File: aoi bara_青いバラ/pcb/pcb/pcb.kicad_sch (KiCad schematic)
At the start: 200 parts, among them J1 OLED_128x64, U1 Raspberry_Pi_Pico

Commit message: deleted:    "aoi bara_\351\235\222\343\201\204\343\203\220\343\203\251/pcb/pcb/#auto_saved_files#" 	deleted:    "aoi bara_\351\235\222\343\201\204\343\203\220\343\203\251/pcb/pcb/_autosave-pcb.kicad_pcb" 	deleted:    "aoi bara_\351\235\222\343\201\204\343\203\220\343\203\251/pcb/pcb/_autosave-pcb.kicad_sch" 	deleted:    "aoi bara_\351\235\222\343\201\204\343\203\220\343\203\251/pcb/pcb/pcb-backups/pcb-2023-12-03_214633.zip" 	new file:   "aoi bara_\351\235\222\343\201\204\343\203\220\343\203\251/pcb/pcb/pcb-backups/pcb-2023-12-03_230541.zip" 	modified:   "aoi bara_\351\235\222\343\201\204\343\203\220\343\203\251/pcb/pcb/pcb.kicad_pcb" 	modified:   "aoi bara_\351\235\222\343\201\204\343\203\220\343\203\251/pcb/pcb/pcb.kicad_prl" 	modified:   "aoi bara_\351\235\222\343\201\204\343\203\220\343\203\251/pcb/pcb/pcb.kicad_pro" 	modified:   "aoi bara_\351\235\222\343\201\204\343\203\220\343\203\251/pcb/pcb/pcb.kicad_sch" 	deleted:    "aoi bara_\351\235\222\343\201\204\343\203\220\343\203\251/pcb/pcb/~_autosave-pcb.kicad_pcb.lck"
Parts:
- removed LED1, LED10, LED11, LED12, LED13, LED14, LED15, LED16, LED17, LED18, LED19, LED2, LED20, LED21, LED22, LED23, LED24, LED25, LED26, LED27, LED28, LED29, LED3, LED30, LED31, LED32, LED33, LED34, LED35, LED36, LED37, LED38, LED39, LED4, LED40, LED41, LED42, LED43, LED44, LED45, LED46, LED47, LED48, LED49, LED5, LED50, LED51, LED52, LED53, LED54, LED55, LED56, LED57, LED58, LED59, LED6, LED60, LED61, LED62, LED63, LED64, LED7, LED8, LED9: LED_WS2812B, LED_SMD:LED_WS2812B_PLCC4_5.0x5.0mm_P3.2mm, symbol ScottoKeebs:LED_WS2812B
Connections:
- no-connect marks 8 -> 7

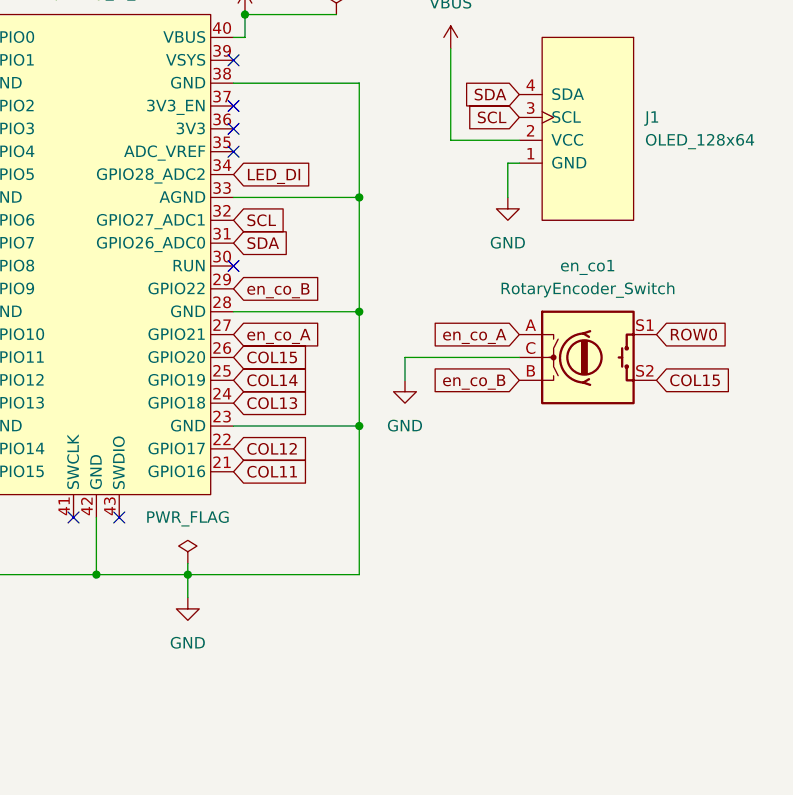
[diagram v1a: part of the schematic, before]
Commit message: deleted:    "aoi bara_\351\235\222\343\201\204\343\203\220\343\203\251/pcb/pcb/#auto_saved_files#" 	deleted:    "aoi bara_\351\235\222\343\201\204\343\203\220\343\203\251/pcb/pcb/_autosave-pcb.kicad_pcb" 	deleted:    "aoi bara_\351\235\222\343\201\204\343\203\220\343\203\251/pcb/pcb/_autosave-pcb.kicad_sch" 	deleted:    "aoi bara_\351\235\222\343\201\204\343\203\220\343\203\251/pcb/pcb/pcb-backups/pcb-2023-11-17_233023.zip" 	new file:   "aoi bara_\351\235\222\343\201\204\343\203\220\343\203\251/pcb/pcb/pcb-backups/pcb-2024-01-28_124537.zip" 	modified:   "aoi bara_\351\235\222\343\201\204\343\203\220\343\203\251/pcb/pcb/pcb.kicad_pcb" 	modified:   "aoi bara_\351\235\222\343\201\204\343\203\220\343\203\251/pcb/pcb/pcb.kicad_prl" 	modified:   "aoi bara_\351\235\222\343\201\204\343\203\220\343\203\251/pcb/pcb/pcb.kicad_pro" 	modified:   "aoi bara_\351\235\222\343\201\204\343\203\220\343\203\251/pcb/pcb/pcb.kicad_sch" 	modified:   "aoi bara_\351\235\222\343\201\204\343\203\220\343\203\251/pcb/pcb/production/pcb-B_Cu.gbr" 	modified:   "aoi bara_\351\235\222\343\201\204\343\203\220\343\203\251/pcb/pcb/production/pcb-B_Mask.gbr" 	modified:   "aoi bara_\351\235\222\343\201\204\343\203\220\343\203\251/pcb/pcb/production/pcb-B_Paste.gbr" 	modified:   "aoi bara_\351\235\222\343\201\204\343\203\220\343\203\251/pcb/pcb/production/pcb-B_Silkscreen.gbr" 	modified:   "aoi bara_\351\235\222\343\201\204\343\203\220\343\203\251/pcb/pcb/production/pcb-Edge_Cuts.gbr" 	modified:   "aoi bara_\351\235\222\343\201\204\343\203\220\343\203\251/pcb/pcb/production/pcb-F_Cu.gbr" 	modified:   "aoi bara_\351\235\222\343\201\204\343\203\220\343\203\251/pcb/pcb/production/pcb-F_Mask.gbr" 	modified:   "aoi bara_\351\235\222\343\201\204\343\203\220\343\203\251/pcb/pcb/production/pcb-F_Paste.gbr" 	modified:   "aoi bara_\351\235\222\343\201\204\343\203\220\343\203\251/pcb/pcb/production/pcb-F_Silkscreen.gbr" 	modified:   "aoi bara_\351\235\222\343\201\204\343\203\220\343\203\251/pcb/pcb/production/pcb-NP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
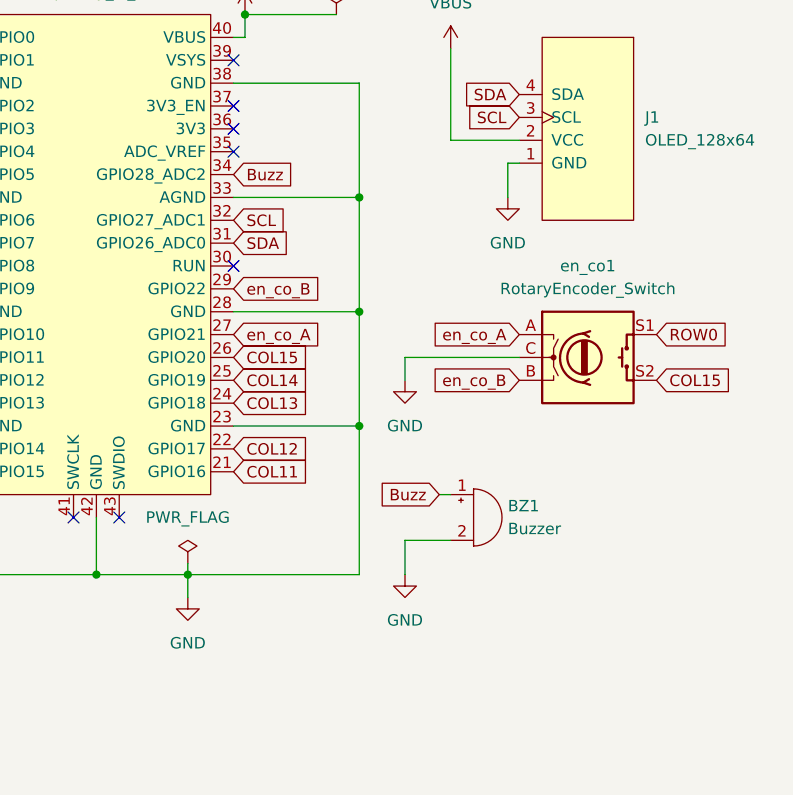
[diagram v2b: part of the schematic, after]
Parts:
- added BZ1: Buzzer, Buzzer_Beeper:Buzzer_12x9.5RM7.6, symbol Device:Buzzer
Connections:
- net GND: now also BZ1.2 (+)
- net LED_DI renamed Buzz
- net Buzz: now also BZ1.1 (-)
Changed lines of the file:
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@@
     (stroke (width 0) (type default))
   )
+  (wire (pts (xy 312.42 99.06) (xy 307.34 99.06))
+    (stroke (width 0) (type default))
+  )
   (wire (pts (xy 196.85 138.43) (xy 196.85 124.46))
     (stroke (width 0) (type default))
@@
     (stroke (width 0) (type default))
   )
+  (wire (pts (xy 311.15 93.98) (xy 312.42 93.98))
+    (stroke (width 0) (type default))
+  )
   (wire (pts (xy 181.61 116.84) (xy 191.77 116.84))
     (stroke (width 0) (type default))
@@
     (stroke (width 0) (type default))
   )
+  (wire (pts (xy 307.34 99.06) (xy 307.34 102.87))
+    (stroke (width 0) (type default))
+  )
   (wire (pts (xy 207.01 124.46) (xy 207.01 138.43))
     (stroke (width 0) (type default))
@@
     )
   )
-  (global_label "LED_DI" (shape input) (at 288.29 58.42 0) (fields_autoplaced)
+  (global_label "Buzz" (shape input) (at 288.29 58.42 0) (fields_autoplaced)
     (effects (font (size 1.27 1.27)) (justify left))
-    (property "Intersheetrefs" "${INTERSHEET_REFS}" (at 297.5647 58.42 0)
+    (property "Intersheetrefs" "${INTERSHEET_REFS}" (at 295.7504 58.42 0)
       (effects (font (size 1.27 1.27)) (justify left) hide)
     )
   )
+  (global_label "Buzz" (shape input) (at 311.15 93.98 180) (fields_autoplaced)
+    (effects (font (size 1.27 1.27)) (justify right))
+    (property "Intersheetrefs" "${INTERSHEET_REFS}" (at 303.6896 93.98 0)
+      (effects (font (size 1.27 1.27)) (justify right) hide)
+    )
+  )
   (global_label "SCL" (shape input) (at 320.04 52.07 180) (fields_autoplaced)
     (effects (font (size 1.27 1.27)) (justify right))
@@
     )
   )
+  (symbol (lib_id "Device:Buzzer") (at 314.96 96.52 0) (unit 1)
+    (in_bom yes) (on_board yes) (dnp no) (fields_autoplaced)
+    (property "Reference" "BZ1" (at 318.77 95.25 0)
+      (effects (font (size 1.27 1.27)) (justify left))
+    )
+    (property "Value" "Buzzer" (at 318.77 97.79 0)
+      (effects (font (size 1.27 1.27)) (justify left))
+    )
+    (property "Footprint" "Buzzer_Beeper:Buzzer_12x9.5RM7.6" (at 314.325 93.98 90)
+      (effects (font (size 1.27 1.27)) hide)
+    )
+    (property "Datasheet" "~" (at 314.325 93.98 90)
+      (effects (font (size 1.27 1.27)) hide)
+    )
+    (pin "1")
+    (pin "2")
+    (instances
+      (project "pcb"
+        (path "/42ebf406-c45a-4349-91ce-22c2a27c1d90"
+          (reference "BZ1") (unit 1)
+        )
+      )
+    )
+  )
   (symbol (lib_id "PCM_marbastlib-mx:MX_SW_HS") (at 168.91 86.36 0) (unit 1)
     (in_bom yes) (on_board yes) (dnp no) (fields_autoplaced)
@@
         )
       )
+    )
+  )
+  (symbol (lib_id "power:GND") (at 307.34 102.87 0) (unit 1)
+    (in_bom yes) (on_board yes) (dnp no) (fields_autoplaced)
+    (property "Reference" "#PWR06" (at 307.34 109.22 0)
+      (effects (font (size 1.27 1.27)) hide)
+    )
+    (property "Value" "GND" (at 307.34 107.95 0)
+      (effects (font (size 1.27 1.27)))
+    )
+    (property "Footprint" "" (at 307.34 102.87 0)
+      (effects (font (size 1.27 1.27)) hide)
+    )
+    (property "Datasheet" "" (at 307.34 102.87 0)
+      (effects (font (size 1.27 1.27)) hide)
+    )
+    (pin "1")
+    (instances
+      (project "pcb"
+        (path "/42ebf406-c45a-4349-91ce-22c2a27c1d90"
+          (reference "#PWR06") (unit 1)
+        )
+      )
